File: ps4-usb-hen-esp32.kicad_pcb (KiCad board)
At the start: 2 copper layers, 54 x 48 mm, 39 parts, among them J1 Micro_SD_Card_Det, J2 USB_B_Micro, J3 Conn_01x06, SW1 SW_Push, SW2 SW_Push, U1 AMS1117-3.3, U2 SRV05-4, U3 ESP32-S2-WROVER

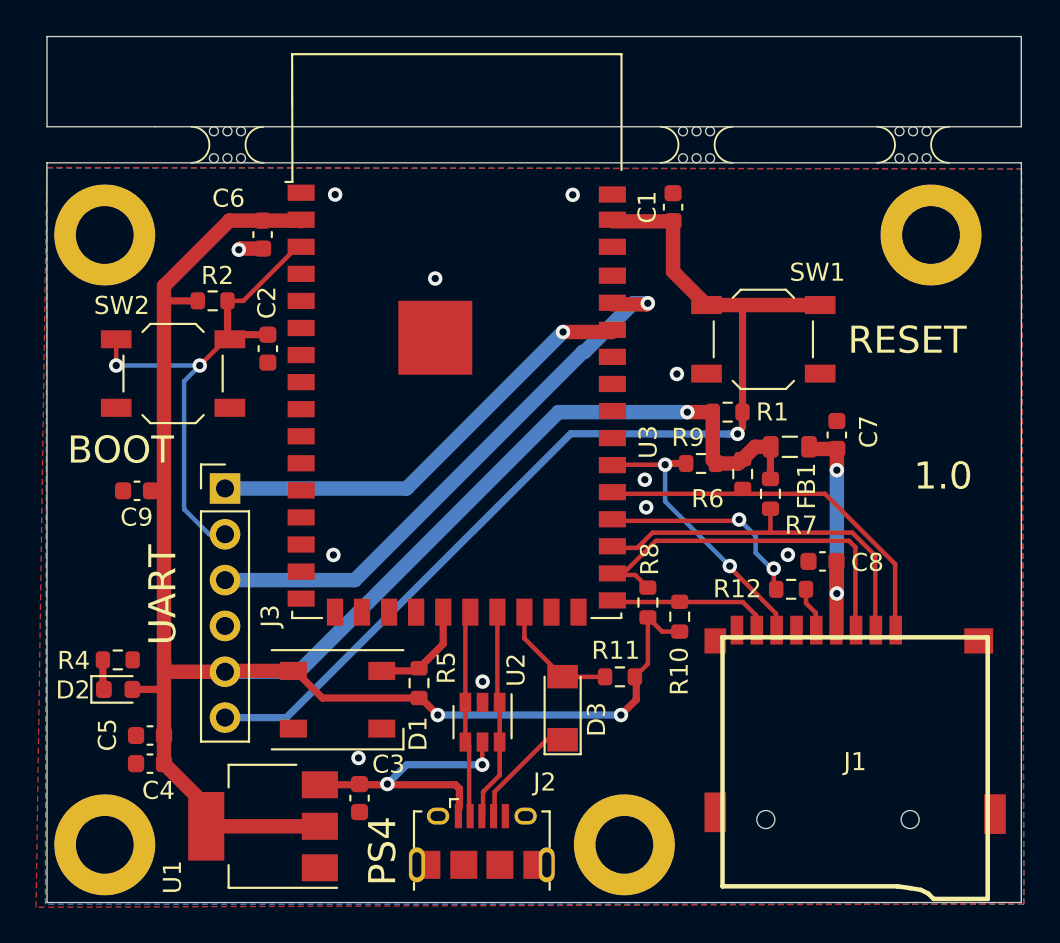
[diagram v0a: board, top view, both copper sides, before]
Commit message: change RGB LED to 5V, add level shifter, change thickness of PCB to 1.0mm, add simple box with FreeCad, update readme
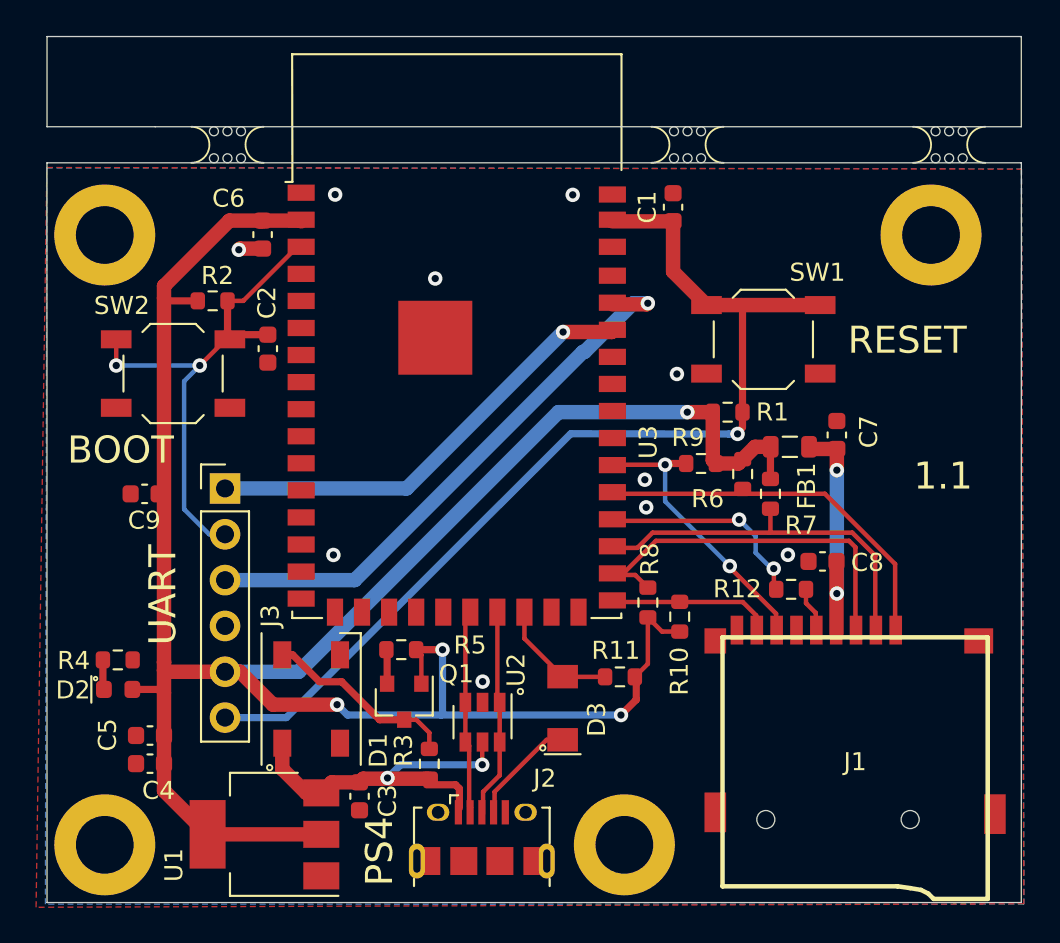
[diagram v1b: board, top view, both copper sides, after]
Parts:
- removed the mouse-bite-2mm-slot at (148.0, 98.0)
- removed the mouse-bite-2mm-slot at (136.0, 98.0)
- added Q1: 2N7002, Package_TO_SOT_SMD:SOT-23, F.Cu at (119.8, 128.9)
- added R3: 10k, R_0603_1608Metric, F.Cu at (121.2, 132.3)
- added mouse-bite-2mm-slot: VAL**, esp32-usb:mouse-bite-2mm-slot, F.Cu at (150.0, 98.0)
- added mouse-bite-2mm-slot: VAL**, esp32-usb:mouse-bite-2mm-slot, F.Cu at (135.5, 98.0)
- FB1: value Ferrite_Bead_Small -> 100MHz/600Ohm/500mA
- U3: value ESP32-S2-WROVER -> ESP32-S2-WROVER-16MB
- moved R5 2.10 mm to (119.6, 126.0), turned to 180 degrees
- moved D1 1.46 mm to (114.6, 128.7), turned to 90 degrees
- moved U1 0.45 mm to (112.0, 136.2)
- moved C9 0.45 mm to (105.4, 117.3)
- moved J2 0.21 mm to (124.1, 136.4)
- moved C3 0.10 mm to (117.3, 134.1)
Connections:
- D1 pad 1: +3V3 -> +5V
- D1 pad 4: /GPIO18 -> /GPIO18_5V
- R5 pad 2: /GPIO18 -> Net-(Q1-Pad2)
- U3 pad 21: /GPIO18 -> (no net)
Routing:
- net /GPIO18_5V: track 0.00 -> 10.8 mm
- net +3V3: track 127.4 -> 134.1 mm, vias 3 -> 4
- net /GPIO18: track 5.70 -> 0.00 mm
- net +5V: track 17.8 -> 20.7 mm
- net Net-(Q1-Pad2): track 0.00 -> 1.90 mm
- net GND: vias 11 -> 10
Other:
- board text added: "1.1"
- board text removed: "1.0"
